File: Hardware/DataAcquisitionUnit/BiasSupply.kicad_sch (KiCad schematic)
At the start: 29 parts, among them Q1 Q_NMOS, U1 TPS7A4901

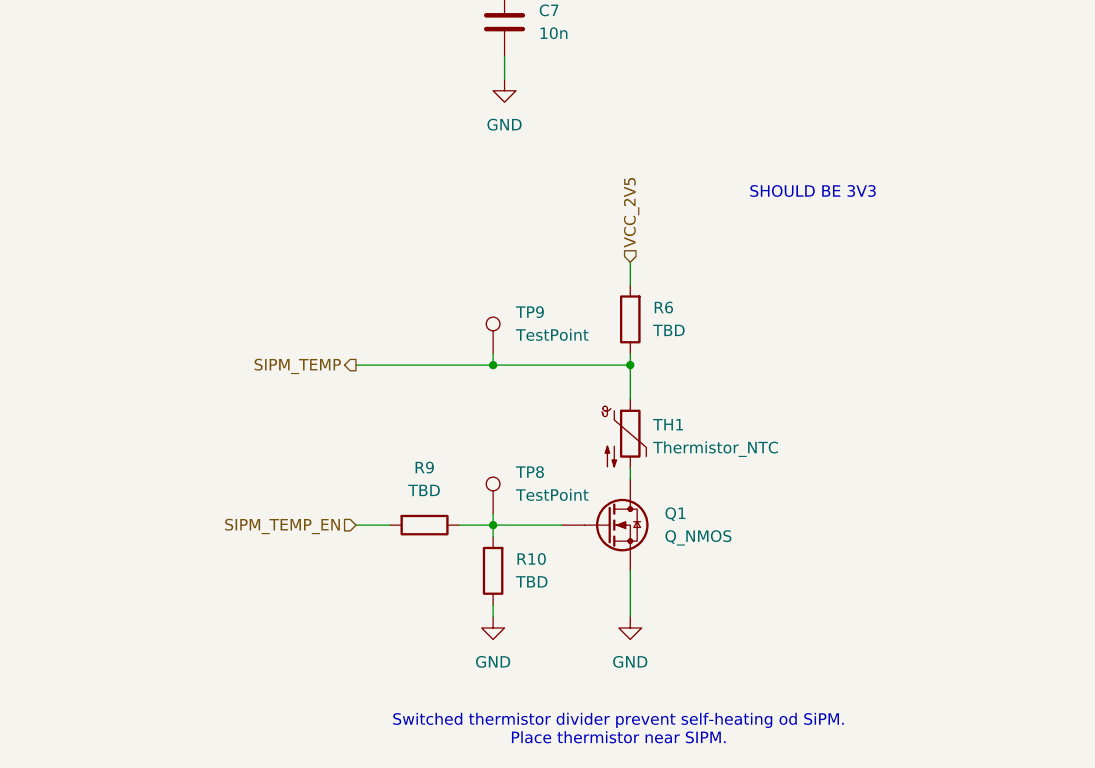
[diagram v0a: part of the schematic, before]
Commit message: fix: #129, fix: #127
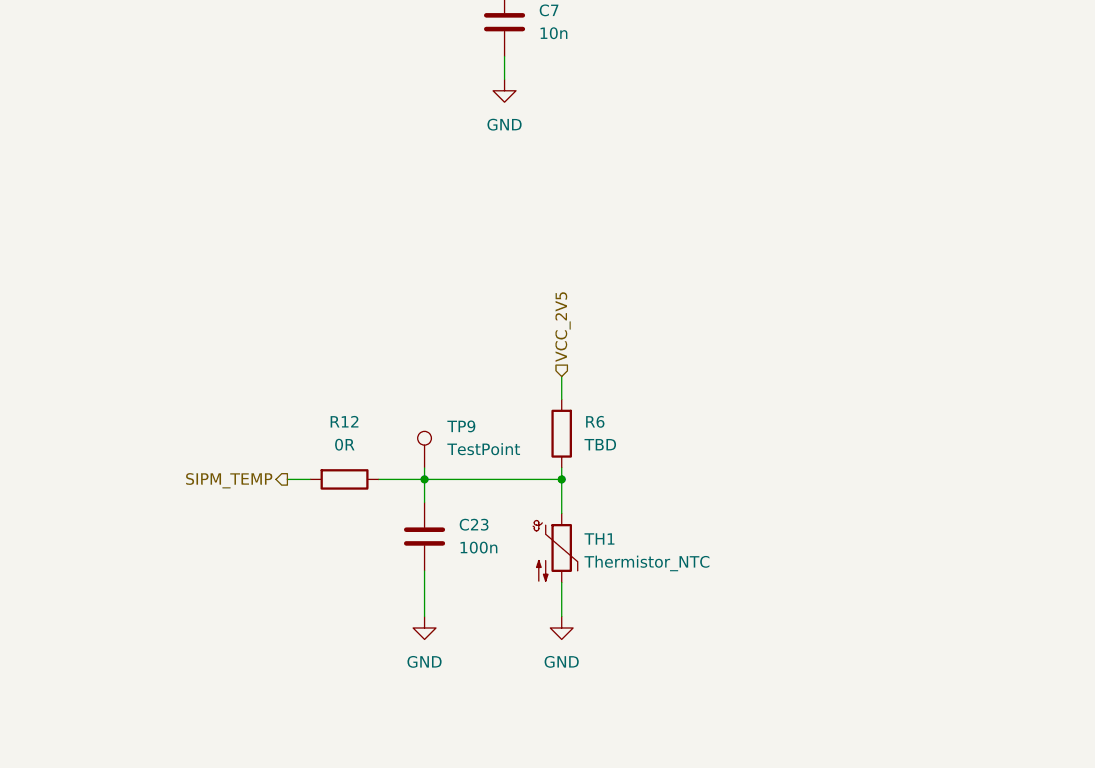
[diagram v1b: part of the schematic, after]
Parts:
- removed Q1: Q_NMOS, symbol Device:Q_NMOS
- removed R10, R9: TBD, Resistor_SMD:R_0805_2012Metric, symbol Device:R
- removed TP8: TestPoint, TestPoint:TestPoint_Pad_D1.5mm, symbol Connector:TestPoint
- added C23: 100n, Capacitor_SMD:C_0805_2012Metric, symbol Device:C
- added R12: 0R, Resistor_SMD:R_0805_2012Metric, symbol Device:R
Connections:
- net GND: now also TH1.2, C23.2
- net SIPM_TEMP: now also R12.2; no longer R6.1, TH1.1, TP9.1
- new net: C23.1, R12.1, R6.1, TH1.1, TP9.1
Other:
- note removed: "SHOULD BE 3V3"
- note removed: "Switched thermistor divider prevent self-heating od SiPM. Place thermistor near SIPM."
- moved on the sheet: R6, TH1, TP9
